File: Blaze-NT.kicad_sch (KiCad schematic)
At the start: 4 parts

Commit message: Addeed part numbers
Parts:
- H1, H2, H3, H4: now not fitted
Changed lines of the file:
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@@
 		(in_bom no)
 		(on_board yes)
-		(dnp no)
+		(dnp yes)
 		(fields_autoplaced yes)
 		(property "Reference" "H4"
@@
 			)
 		)
+		(property "LCSC" ""
+			(at 248.92 138.43 0)
+			(effects
+				(font
+					(size 1.27 1.27)
+				)
+				(hide yes)
+			)
+		)
 		(pin "1"
 		)
@@
 		(in_bom no)
 		(on_board yes)
-		(dnp no)
+		(dnp yes)
 		(fields_autoplaced yes)
 		(property "Reference" "H1"
@@
 			)
 		)
+		(property "LCSC" ""
+			(at 226.06 138.43 0)
+			(effects
+				(font
+					(size 1.27 1.27)
+				)
+				(hide yes)
+			)
+		)
 		(pin "1"
 		)
@@
 		(in_bom no)
 		(on_board yes)
-		(dnp no)
+		(dnp yes)
 		(fields_autoplaced yes)
 		(property "Reference" "H2"
@@
 			)
 		)
+		(property "LCSC" ""
+			(at 233.68 138.43 0)
+			(effects
+				(font
+					(size 1.27 1.27)
+				)
+				(hide yes)
+			)
+		)
 		(pin "1"
 		)
@@
 		(in_bom no)
 		(on_board yes)
-		(dnp no)
+		(dnp yes)
 		(fields_autoplaced yes)
 		(property "Reference" "H3"
@@
 			(at 241.3 138.43 0)
 			(effects
+				(font
+					(size 1.27 1.27)
+				)
+				(hide yes)
+			)
+		)
+		(property "LCSC" ""
+			(at 241.3 138.43 0)
+			(effects

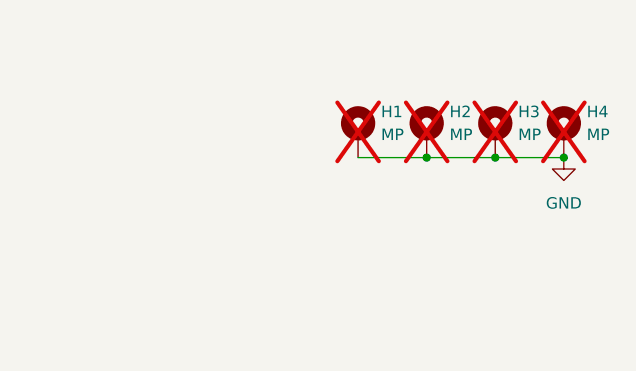
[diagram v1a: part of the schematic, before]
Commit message: Added fiducials
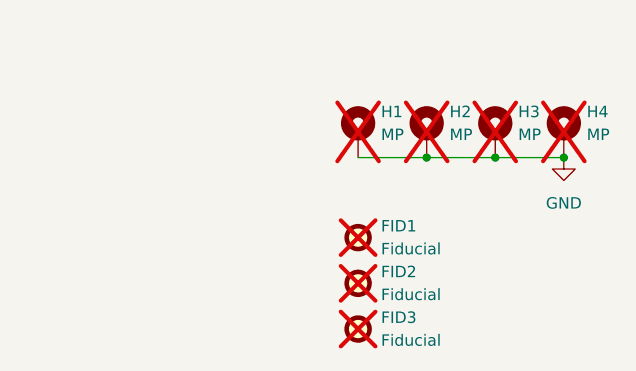
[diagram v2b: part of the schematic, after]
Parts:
- added FID1, FID2, FID3: Fiducial, Avionics_Feet:JLC_Fiducial, symbol Mechanical:Fiducial
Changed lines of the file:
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@@
+	)
+	(symbol
+		(lib_id "Mechanical:Fiducial")
+		(at 226.06 160.02 0)
+		(unit 1)
+		(exclude_from_sim no)
+		(in_bom no)
+		(on_board yes)
+		(dnp yes)
+		(fields_autoplaced yes)
+		(property "Reference" "FID3"
+			(at 228.6 158.7499 0)
+			(effects
+				(font
+					(size 1.27 1.27)
+				)
+				(justify left)
+			)
+		)
+		(property "Value" "Fiducial"
+			(at 228.6 161.2899 0)
+			(effects
+				(font
+					(size 1.27 1.27)
+				)
+				(justify left)
+			)
+		)
+		(property "Footprint" "Avionics_Feet:JLC_Fiducial"
+			(at 226.06 160.02 0)
+			(effects
+				(font
+					(size 1.27 1.27)
+				)
+				(hide yes)
+			)
+		)
+		(property "Datasheet" "~"
+			(at 226.06 160.02 0)
+			(effects
+				(font
+					(size 1.27 1.27)
+				)
+				(hide yes)
+			)
+		)
+		(property "Description" "Fiducial Marker"
+			(at 226.06 160.02 0)
+			(effects
+				(font
+					(size 1.27 1.27)
+				)
+				(hide yes)
+			)
+		)
+		(instances
+			(project "Blaze-NT"
+				(path "/2c2eadf0-5503-4531-8753-1a232087fe8c"
+					(reference "FID3")
+					(unit 1)
+				)
+			)
+		)
 	)
 	(symbol
@@
 					(unit 1)
 				)
+			)
+		)
+	)
+	(symbol
+		(lib_id "Mechanical:Fiducial")
+		(at 226.06 154.94 0)
+		(unit 1)
+		(exclude_from_sim no)
+		(in_bom no)
+		(on_board yes)
+		(dnp yes)
+		(fields_autoplaced yes)
+		(property "Reference" "FID2"
+			(at 228.6 153.6699 0)
+			(effects
+				(font
+					(size 1.27 1.27)
+				)
+				(justify left)
+			)
+		)
+		(property "Value" "Fiducial"
+			(at 228.6 156.2099 0)
+			(effects
+				(font
+					(size 1.27 1.27)
+				)
+				(justify left)
+			)
+		)
+		(property "Footprint" "Avionics_Feet:JLC_Fiducial"
+			(at 226.06 154.94 0)
+			(effects
+				(font
+					(size 1.27 1.27)
+				)
+				(hide yes)
+			)
+		)
+		(property "Datasheet" "~"
+			(at 226.06 154.94 0)
+			(effects
+				(font
+					(size 1.27 1.27)
+				)
+				(hide yes)
+			)
+		)
+		(property "Description" "Fiducial Marker"
+			(at 226.06 154.94 0)
+			(effects
+				(font
+					(size 1.27 1.27)
+				)
+				(hide yes)
+			)
+		)
+		(instances
+			(project "Blaze-NT"
+				(path "/2c2eadf0-5503-4531-8753-1a232087fe8c"
+					(reference "FID2")
+					(unit 1)
+				)
+			)
+		)
+	)
+	(symbol
+		(lib_id "Mechanical:Fiducial")
+		(at 226.06 149.86 0)
+		(unit 1)
+		(exclude_from_sim no)
+		(in_bom no)
+		(on_board yes)
+		(dnp yes)
+		(fields_autoplaced yes)
+		(property "Reference" "FID1"
+			(at 228.6 148.5899 0)
+			(effects
+				(font
+					(size 1.27 1.27)
+				)
+				(justify left)
+			)
+		)
+		(property "Value" "Fiducial"
+			(at 228.6 151.1299 0)
+			(effects
+				(font
+					(size 1.27 1.27)
+				)
+				(justify left)
+			)
+		)
+		(property "Footprint" "Avionics_Feet:JLC_Fiducial"
+			(at 226.06 149.86 0)
+			(effects
+				(font
+					(size 1.27 1.27)
+				)
+				(hide yes)
+			)
+		)
+		(property "Datasheet" "~"
+			(at 226.06 149.86 0)
+			(effects
+				(font
+					(size 1.27 1.27)
+				)
+				(hide yes)
+			)
+		)
+		(property "Description" "Fiducial Marker"
+			(at 226.06 149.86 0)
+			(effects
+				(font
+					(size 1.27 1.27)
+				)
+				(hide yes)
+			)
+		)
+		(instances
+			(project ""
+				(path "/2c2eadf0-5503-4531-8753-1a232087fe8c"
+					(reference "FID1")
+					(unit 1)
+				)
